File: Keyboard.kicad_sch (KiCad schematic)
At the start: 35 parts, among them SW1 SW_Push, SW10 SW_Push, SW11 SW_Push, SW12 SW_Push, SW13 SW_Push, SW14 SW_Push, SW15 SW_Push, SW16 SW_Push, SW2 SW_Push, SW3 SW_Push, SW4 SW_Push, SW5 SW_Push, SW6 SW_Push, SW7 SW_Push, SW8 SW_Push, SW9 SW_Push, U1 XIAO-nRF52840-SMD

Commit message: First schematic design
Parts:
- added H1, H2, H3, H4, H5: MountingHole, symbol Mechanical:MountingHole
- added R1: 806K, symbol Device:R
- added R2: 2M, symbol Device:R
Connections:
- net GND: now also R2.1
- net VBAT: now also U1.15 (BAT), R1.2
- net BT_PIN: now reaches U1.1 (P0.02_A0_D0)
- net BT_PIN: now also R1.1, R2.2
- no-connect marks 0 -> 10
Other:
- moved on the sheet: D1, D10, D11, D12, D13, D14, D15, D16, D2, D3, D4, D5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

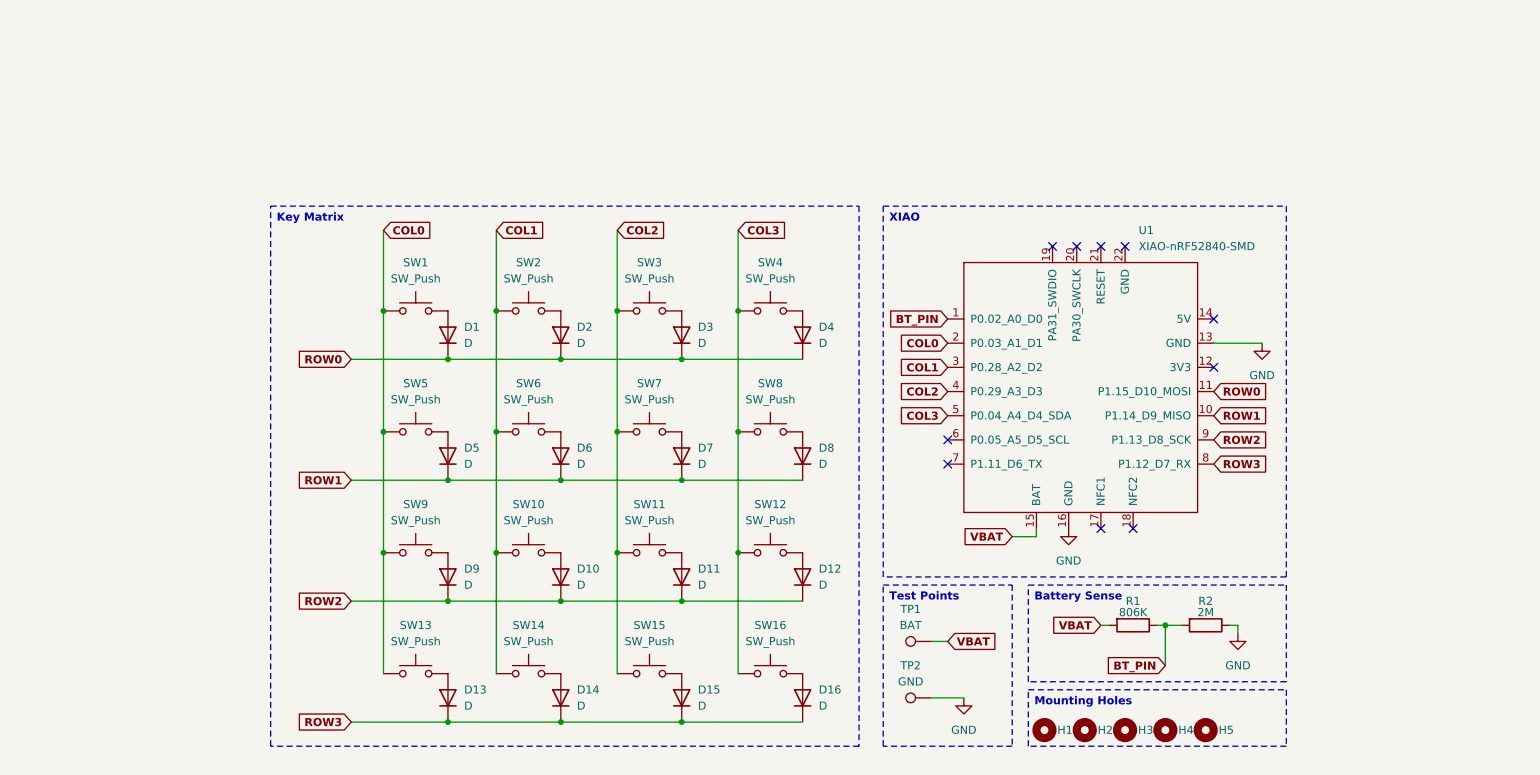
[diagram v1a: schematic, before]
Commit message: Finished the schematics without LEDs
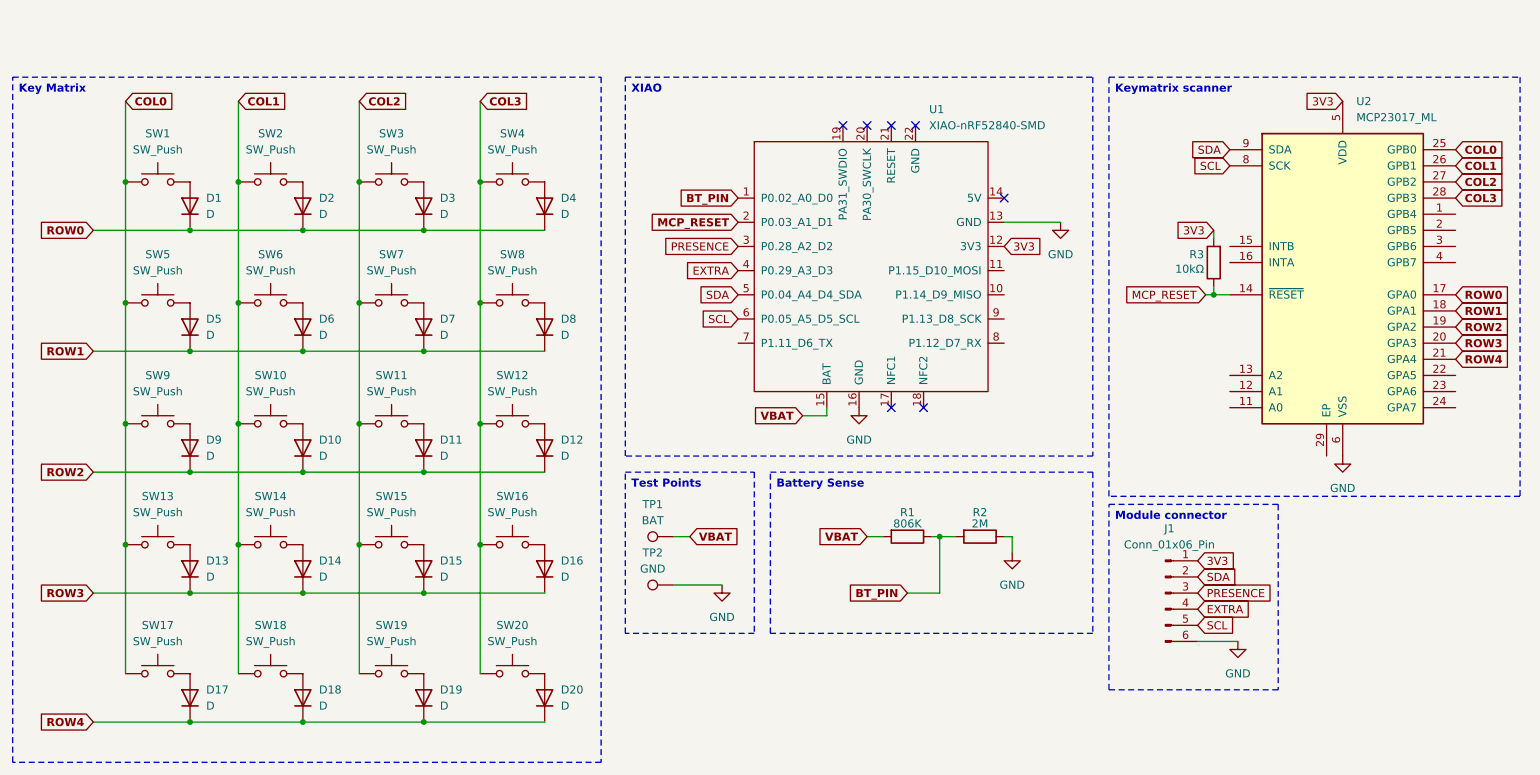
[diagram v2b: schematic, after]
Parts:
- removed H1, H2, H3, H4, H5: MountingHole, symbol Mechanical:MountingHole
- added D17, D18, D19, D20: D, Diode_SMD:D_SOD-123, symbol Device:D
- added J1: Conn_01x06_Pin, symbol Connector:Conn_01x06_Pin
- added R3: 10kΩ, symbol Device:R
- added SW17, SW18, SW19, SW20: SW_Push, Button_Switch_Keyboard:SW_Cherry_MX_1.00u_PCB, symbol Switch:SW_Push
- added U2: MCP23017_ML, Package_DFN_QFN:QFN-28-1EP_6x6mm_P0.65mm_EP4.25x4.25mm, symbol Interface_Expansion:MCP23017_ML
- D1, D10, D11, D12, D13, D14, D15, D16, D2, D3, D4, D5, D6, D7, D8, D9: footprint (none) -> Diode_SMD:D_SOD-123
- R1, R2: footprint (none) -> Resistor_SMD:R_0805_2012Metric
- SW1, SW10, SW11, SW12, SW13, SW14, SW15, SW16, SW2, SW3, SW4, SW5, SW6, SW7, SW8, SW9: footprint (none) -> Button_Switch_Keyboard:SW_Cherry_MX_1.00u_PCB
- TP1, TP2: footprint (none) -> TestPoint:TestPoint_Pad_D2.0mm
- U1: footprint (none) -> Seeed Studio XIAO Series Library:modified-XIAO-nRF52840-SMD
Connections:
- net COL0: now also SW17.1, U2.25 (GPB0); no longer U1.2 (P0.03_A1_D1)
- net COL1: now also SW18.1, U2.26 (GPB1); no longer U1.3 (P0.28_A2_D2)
- net COL2: now also SW19.1, U2.27 (GPB2); no longer U1.4 (P0.29_A3_D3)
- net COL3: now also SW20.1, U2.28 (GPB3); no longer U1.5 (P0.04_A4_D4_SDA)
- net GND: now also J1.6 (Pin_6), U2.6 (VSS)
- net ROW0: now also U2.17 (GPA0); no longer U1.11 (P1.15_D10_MOSI)
- net ROW1: now also U2.18 (GPA1); no longer U1.10 (P1.14_D9_MISO)
- net ROW2: now also U2.19 (GPA2); no longer U1.9 (P1.13_D8_SCK)
- net ROW3: now also U2.20 (GPA3); no longer U1.8 (P1.12_D7_RX)
- net 3V3: now reaches U1.12 (3V3)
- net 3V3: now also J1.1 (Pin_1), R3.2, U2.5 (VDD)
- net SCL: now reaches U1.6 (P0.05_A5_D5_SCL)
- net SCL: now also J1.5 (Pin_5), U2.8 (SCK)
- new net: D18.2 (A), SW18.2
- new net: D19.2 (A), SW19.2
- new net: D17.2 (A), SW17.2
- new net: D20.2 (A), SW20.2
- new net EXTRA: J1.4 (Pin_4), U1.4 (P0.29_A3_D3)
- new net MCP_RESET: R3.1, U1.2 (P0.03_A1_D1), U2.14 (~{RESET})
- new net PRESENCE: J1.3 (Pin_3), U1.3 (P0.28_A2_D2)
- new net ROW4: D17.1 (K), D18.1 (K), D19.1 (K), D20.1 (K), U2.21 (GPA4)
- new net SDA: J1.2 (Pin_2), U1.5 (P0.04_A4_D4_SDA), U2.9 (SDA)
- no-connect marks 10 -> 7
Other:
- moved on the sheet: D1, D10, D11, D12, D13, D14, D15, D16, D2, D3, D4, D5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

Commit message: Rearranged the key matrix and rotated the MCP
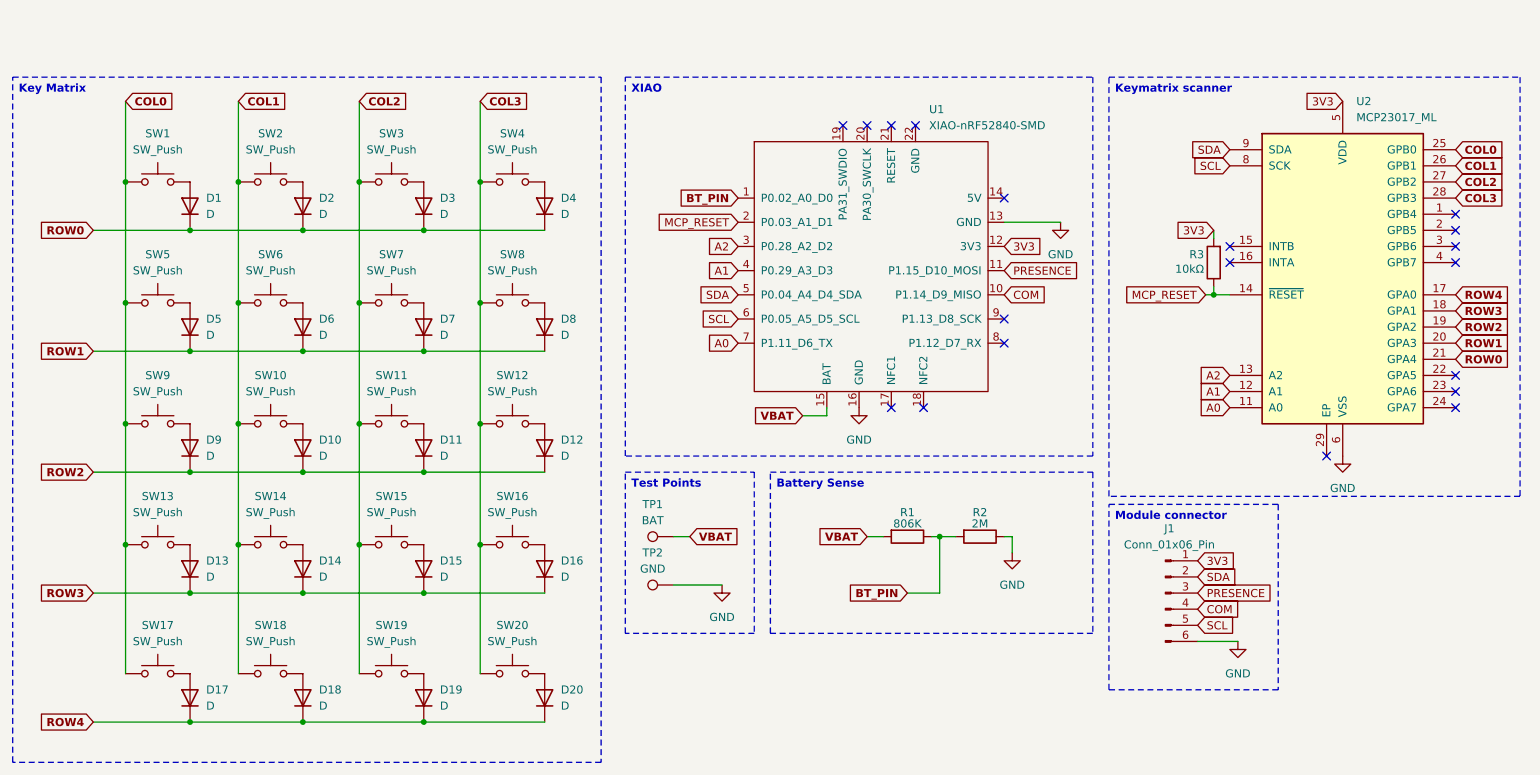
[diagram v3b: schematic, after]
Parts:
- J1: footprint (none) -> Connector_Pin:Pin_D1.2mm_L10.2mm_W2.9mm_FlatFork
- R3: footprint (none) -> Resistor_SMD:R_0805_2012Metric
- SW1, SW10, SW11, SW12, SW13, SW14, SW15, SW16, SW17, SW18, SW19, SW2, SW20, SW3, SW4, SW5, SW6, SW7, SW8, SW9: footprint Button_Switch_Keyboard:SW_Cherry_MX_1.00u_PCB -> PCM_marbastlib-xp-choc:SW_choc_v2_HS_CPG135001S30_1u
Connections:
- net PRESENCE: now also U1.11 (P1.15_D10_MOSI); no longer U1.3 (P0.28_A2_D2)
- net ROW0: now also U2.21 (GPA4); no longer U2.17 (GPA0)
- net ROW1: now also U2.20 (GPA3); no longer U2.18 (GPA1)
- net ROW3: now also U2.18 (GPA1); no longer U2.20 (GPA3)
- net ROW4: now also U2.17 (GPA0); no longer U2.21 (GPA4)
- net A0: now reaches U2.11 (A0)
- net A0: now also U1.7 (P1.11_D6_TX)
- net A1: now reaches U2.12 (A1)
- net A1: now also U1.4 (P0.29_A3_D3)
- net A2: now reaches U2.13 (A2)
- net A2: now also U1.3 (P0.28_A2_D2)
- net COM: now reaches U1.10 (P1.14_D9_MISO)
- net COM: now also J1.4 (Pin_4)
- removed net EXTRA: J1.4 (Pin_4), U1.4 (P0.29_A3_D3)
- no-connect marks 7 -> 19

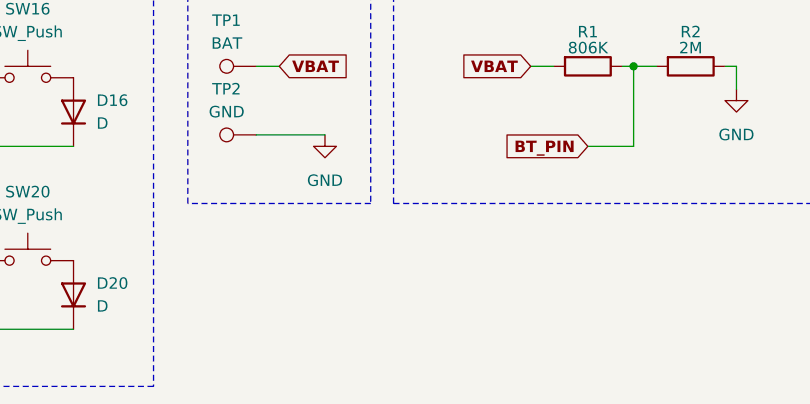
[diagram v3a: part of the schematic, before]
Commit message: Add: mounting holes
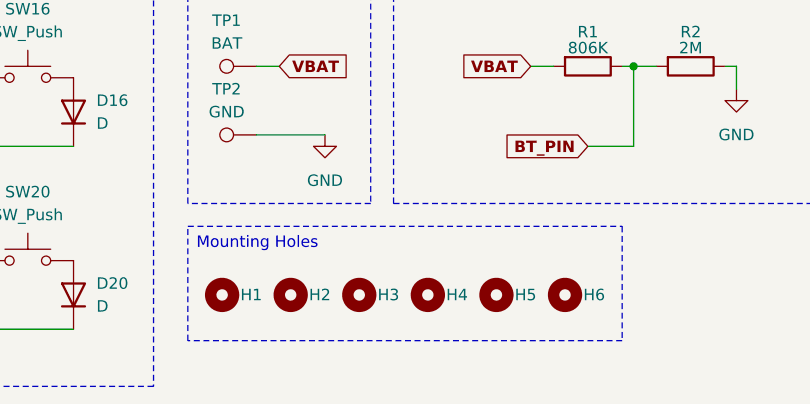
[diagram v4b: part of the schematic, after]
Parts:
- added H1, H2, H3, H4, H5, H6: MountingHole, MountingHole:MountingHole_2.2mm_M2, symbol Mechanical:MountingHole

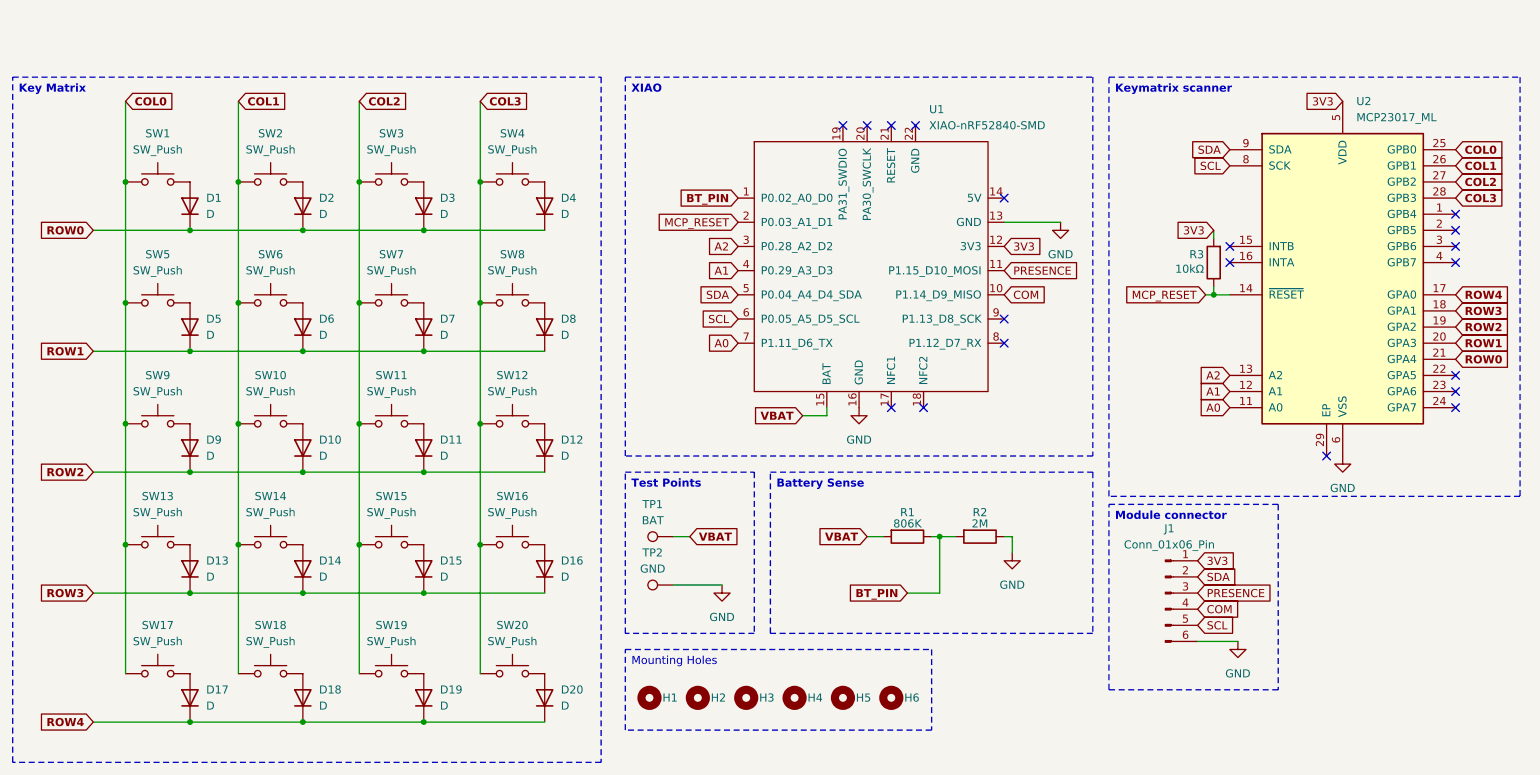
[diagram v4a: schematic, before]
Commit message: Add: modular connectors
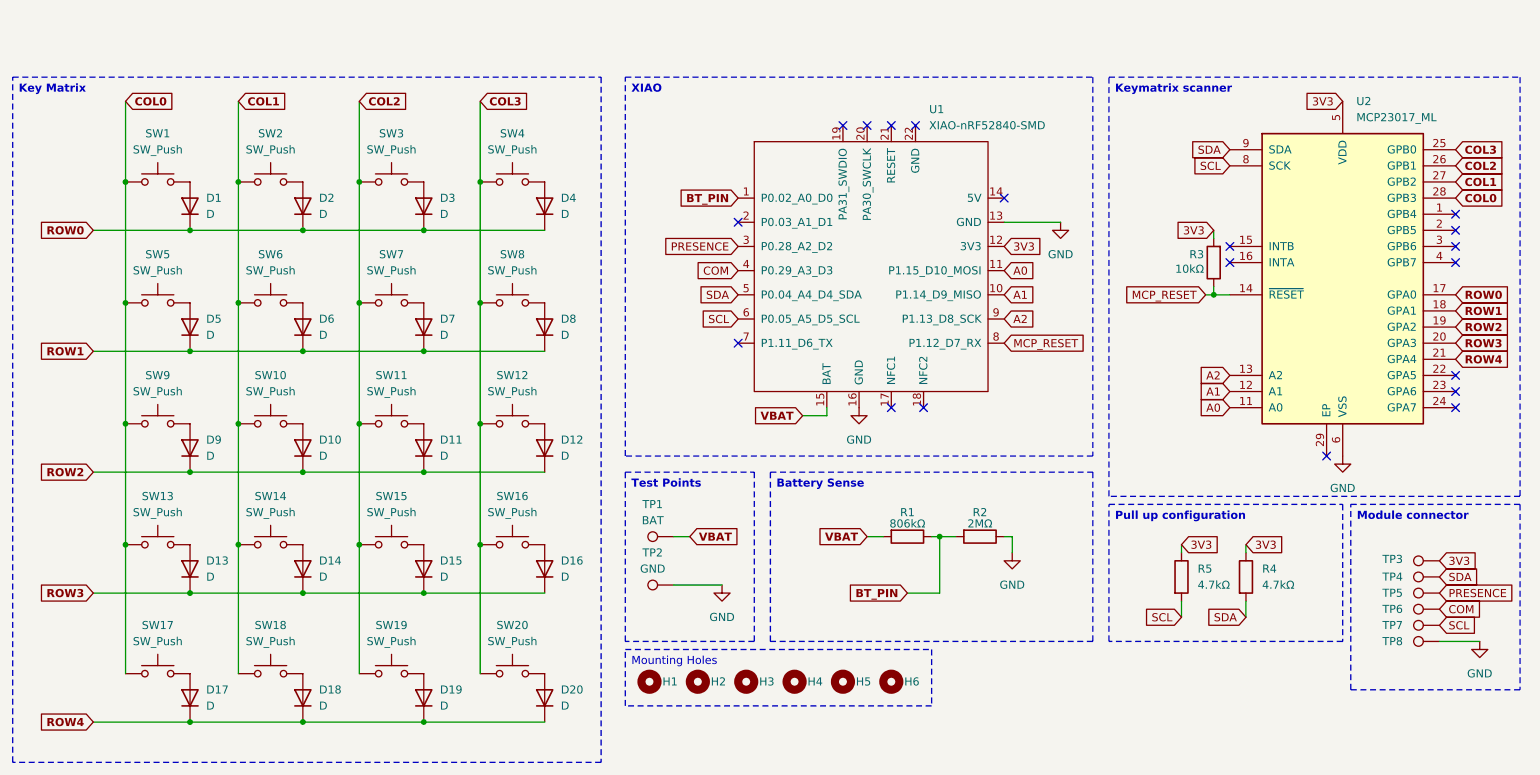
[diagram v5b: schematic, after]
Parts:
- removed J1: Conn_01x06_Pin, Connector_Pin:Pin_D1.2mm_L10.2mm_W2.9mm_FlatFork, symbol Connector:Conn_01x06_Pin
- added R4, R5: 4.7kΩ, Resistor_SMD:R_0805_2012Metric, symbol Device:R
- added TP3, TP4, TP5, TP6, TP7, TP8: TestPoint, TestPoint:TestPoint_Pad_D2.0mm, symbol Connector:TestPoint
- R1: value 806K -> 806kΩ
- R2: value 2M -> 2MΩ
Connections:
- net 3V3: now also R4.1, R5.1, TP3.1
- net A0: now also U1.11 (P1.15_D10_MOSI); no longer U1.7 (P1.11_D6_TX)
- net A1: now also U1.10 (P1.14_D9_MISO); no longer U1.4 (P0.29_A3_D3)
- net A2: now also U1.9 (P1.13_D8_SCK); no longer U1.3 (P0.28_A2_D2)
- net COL0: now also U2.28 (GPB3); no longer U2.25 (GPB0)
- net COL1: now also U2.27 (GPB2); no longer U2.26 (GPB1)
- net COL2: now also U2.26 (GPB1); no longer U2.27 (GPB2)
- net COL3: now also U2.25 (GPB0); no longer U2.28 (GPB3)
- net COM: now also U1.4 (P0.29_A3_D3), TP6.1; no longer U1.10 (P1.14_D9_MISO)
- net GND: now also TP8.1
- net MCP_RESET: now also U1.8 (P1.12_D7_RX); no longer U1.2 (P0.03_A1_D1)
- net PRESENCE: now also U1.3 (P0.28_A2_D2), TP5.1; no longer U1.11 (P1.15_D10_MOSI)
- net ROW0: now also U2.17 (GPA0); no longer U2.21 (GPA4)
- net ROW1: now also U2.18 (GPA1); no longer U2.20 (GPA3)
- net ROW3: now also U2.20 (GPA3); no longer U2.18 (GPA1)
- net ROW4: now also U2.21 (GPA4); no longer U2.17 (GPA0)
- net SCL: now also R5.2, TP7.1
- net SDA: now also R4.2, TP4.1
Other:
- moved on the sheet: H1, H2, H3, H4, H5, H6
